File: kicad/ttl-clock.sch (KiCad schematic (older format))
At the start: 9 parts

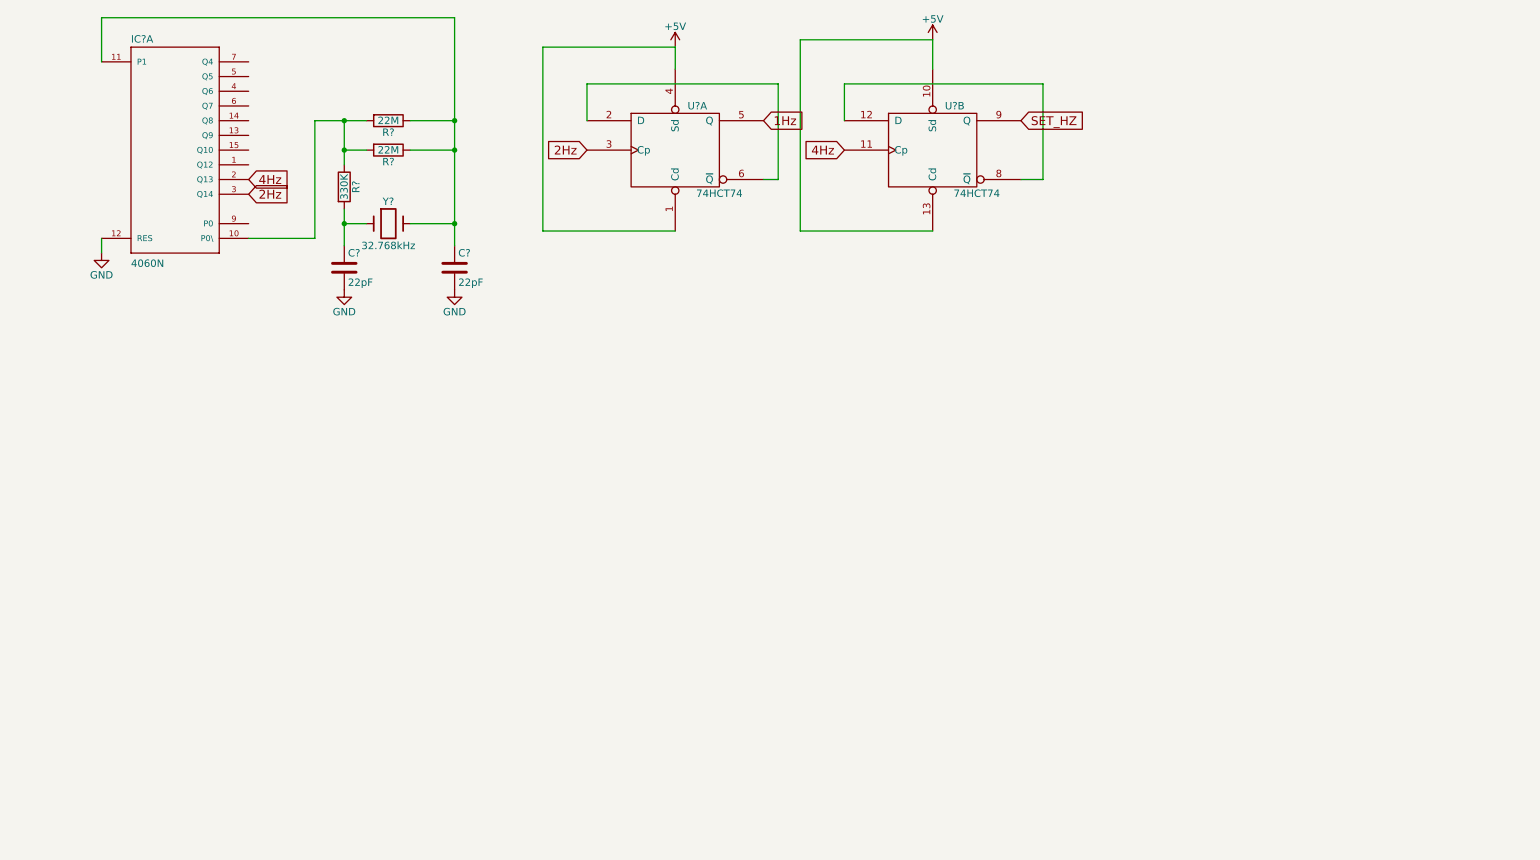
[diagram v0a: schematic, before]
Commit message: Add buttons logic
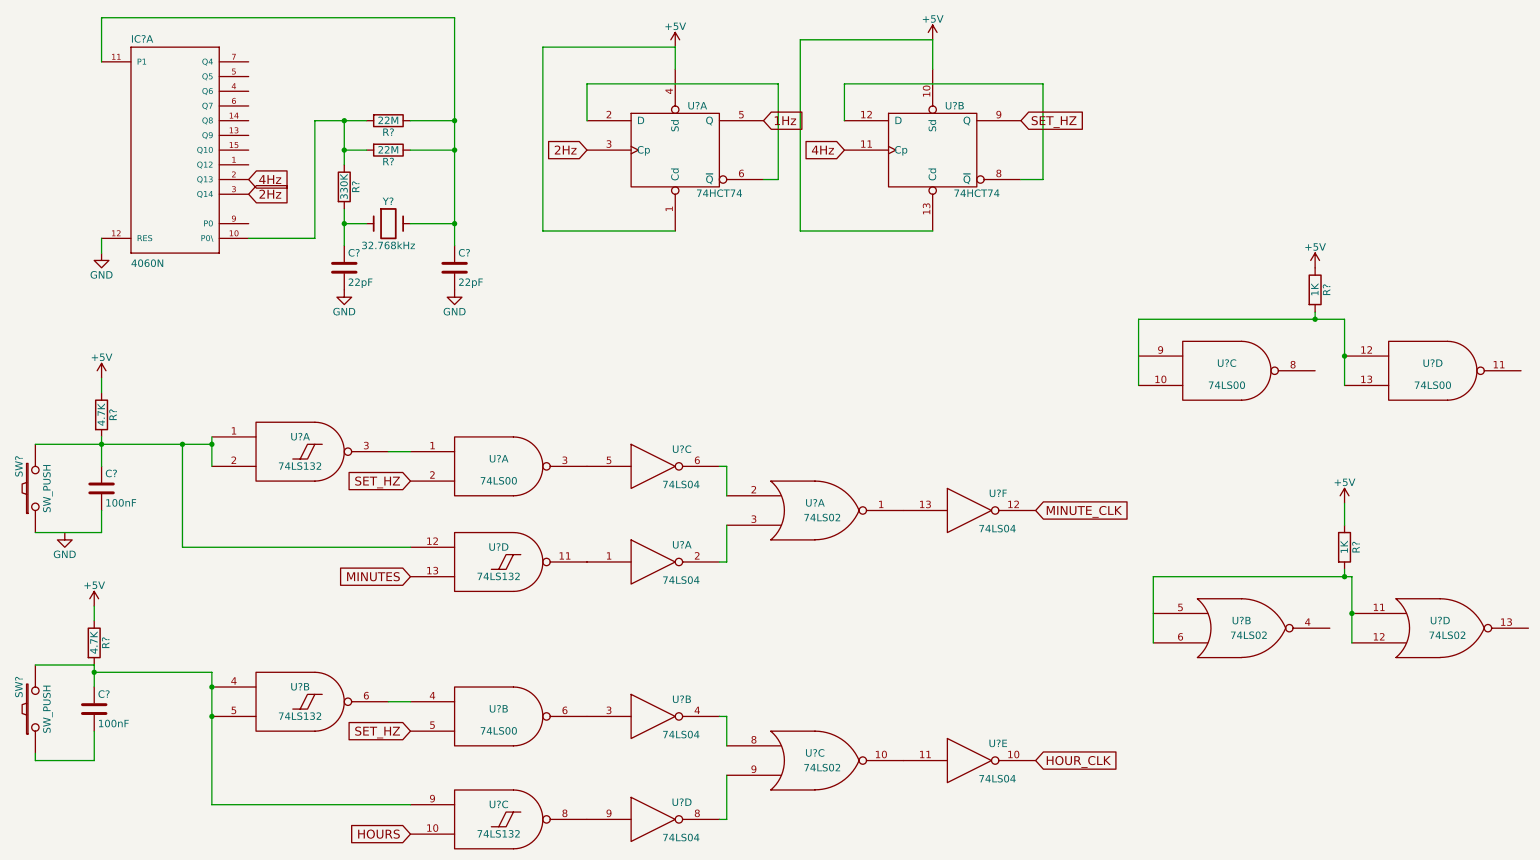
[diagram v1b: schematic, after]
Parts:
- added C? (x2): 100nF, symbol C
- added R? (x2): 4.7K, symbol R
- added R? (x2): 1K, symbol R
- added SW? (x2): SW_PUSH, symbol SW_PUSH
- added U? (x4): 74LS132, symbol 74LS132
- added U? (x6): 74LS04, symbol 74LS04
- added U? (x4): 74LS02, symbol 74LS02
- added U? (x4): 74LS00, symbol 74LS00
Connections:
- net +5V: now also R?.1, R?.1, R?.1, R?.1
- net GND: now also U?.7 (GND), U?.7 (GND), U?.7 (GND), U?.7 (GND), U?.7 (GND), U?.7 (GND), U?.7 (GND), U?.7 (GND), U?.7 (GND), U?.7 (GND), U?.7 (GND), U?.7 (GND), U?.7 (GND), U?.7 (GND), U?.7 (GND), U?.7 (GND), U?.7 (GND), U?.7 (GND)
- net SET_HZ: now also U?.2, U?.5
- net VCC: now also U?.14 (VCC), U?.14 (VCC), U?.14 (VCC), U?.14 (VCC), U?.14 (VCC), U?.14 (VCC), U?.14 (VCC), U?.14 (VCC), U?.14 (VCC), U?.14 (VCC), U?.14 (VCC), U?.14 (VCC), U?.14 (VCC), U?.14 (VCC), U?.14 (VCC), U?.14 (VCC), U?.14 (VCC), U?.14 (VCC)
- new net: C?.1, R?.2, SW?.2, U?.1, U?.12, U?.2
- new net: U?.1, U?.3
- new net: C?.1, R?.2, SW?.2, U?.4, U?.5, U?.9
- new net: U?.4, U?.6
- new net: U?.8, U?.9 (x2)
- new net: U?.1, U?.11
- new net: C?.2, SW?.1 (x2)
- new net: U?.2, U?.3
- new net: U?.3, U?.6
- new net: U?.4, U?.8
- new net: U?.3, U?.5
- new net: U?.2, U?.6
- new net: U?.10, U?.11
- new net: U?.1, U?.13
- new net: R?.2, U?.11, U?.12, U?.6
- new net: R?.2, U?.10, U?.12, U?.13
- new net HOURS: U?.10
- new net HOUR_CLK: U?.10
- new net MINUTES: U?.13
- new net MINUTE_CLK: U?.12

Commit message: seconds section
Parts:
- removed C? (x2): 22pF, symbol C
- removed C? (x2): 100nF, symbol C
- removed IC?: 4060N, 40xx-DIL16, symbol 4060N
- removed R? (x2): 22M, symbol R
- removed R?: 330K, symbol R
- removed R? (x2): 4.7K, symbol R
- removed R? (x2): 1K, symbol R
- removed SW? (x2): SW_PUSH, symbol SW_PUSH
- removed U? (x2): 74HCT74, symbol 74HCT74
- removed U? (x4): 74LS132, symbol 74LS132
- removed U? (x6): 74LS04, symbol 74LS04
- removed U? (x4): 74LS02, symbol 74LS02
- removed U? (x4): 74LS00, symbol 74LS00
- removed Y?: 32.768kHz, symbol Crystal

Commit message: minute segment
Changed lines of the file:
@@
 F1 "frequency-and-set-buttons.sch" 60
 $EndSheet
-Text HLabel 3100 1450 0    60   Output ~ 0
+Text HLabel 3100 1750 0    60   Output ~ 0
 MINUTE_CLK
-Text HLabel 3100 1750 0    60   Output ~ 0
+Text HLabel 3100 1500 0    60   Output ~ 0
 HOUR_CLK
 Text HLabel 3100 2000 0    60   Output ~ 0
@@
 Wire Wire Line
 	1050 1550 1250 1550
+Text HLabel 3450 3600 2    60   Input ~ 0
+MINUTE_CLK
+Text HLabel 3450 3900 2    60   Output ~ 0
+HOUR_PULSE
+Wire Wire Line
+	3450 3600 3350 3600
+Wire Wire Line
+	3450 3900 3100 3900
+Wire Wire Line
+	3100 3900 3100 2800
+Wire Wire Line
+	3100 2800 1150 2800
+Wire Wire Line
+	1150 2800 1150 1850
+Wire Wire Line
+	1150 1850 1250 1850
+Wire Wire Line
+	3350 3600 3350 1750
+Wire Wire Line
+	3350 1750 3100 1750
 $EndSCHEMATC

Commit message: hours section
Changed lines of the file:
@@
 Wire Wire Line
 	3350 1750 3100 1750
+Text HLabel 5900 3600 2    60   Input ~ 0
+HOUR_CLK
+Wire Wire Line
+	5900 3600 5700 3600
+Wire Wire Line
+	5700 3600 5700 1500
+Wire Wire Line
+	5700 1500 3100 1500
 $EndSCHEMATC
